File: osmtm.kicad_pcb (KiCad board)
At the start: 2 copper layers, 144.8 x 76.2 mm, 15 parts

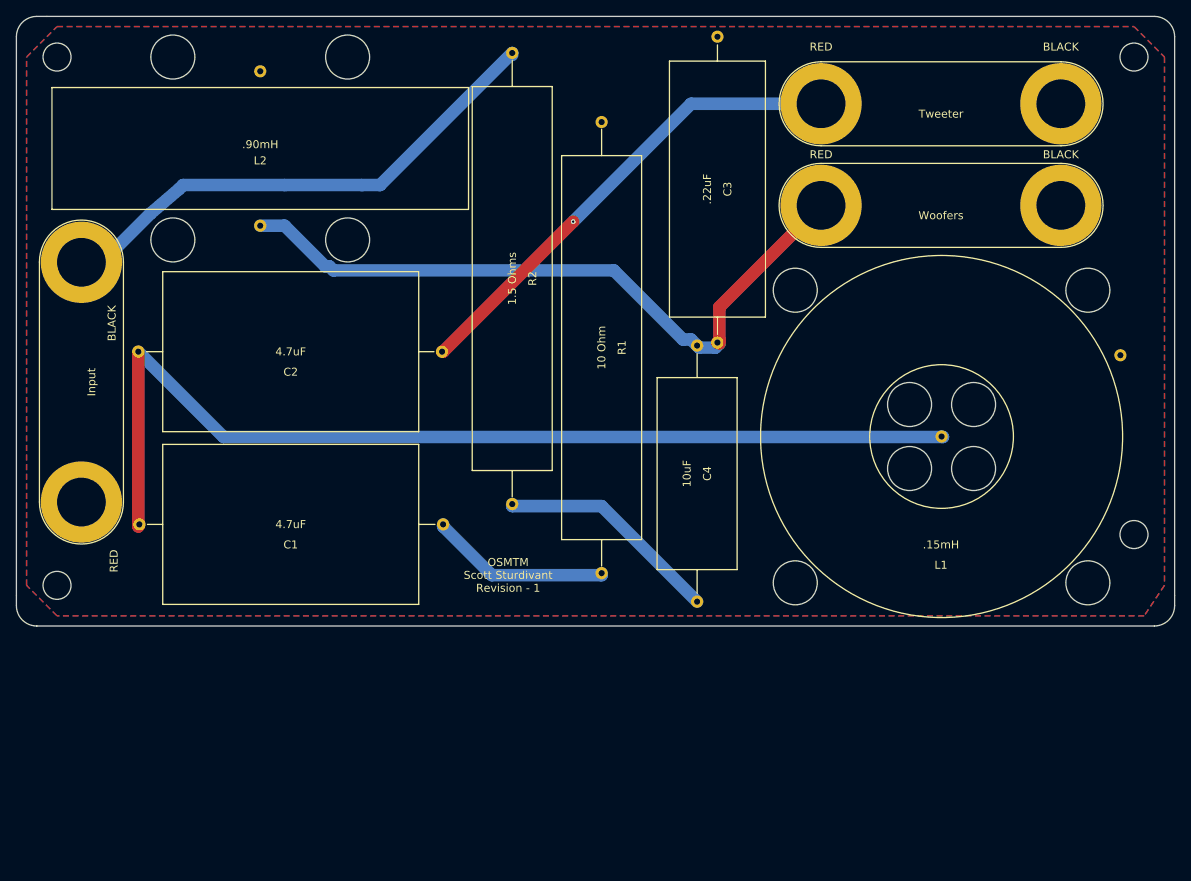
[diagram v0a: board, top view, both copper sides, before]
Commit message: Use screw terminals, increase trace width.
The trace width was incorrectly using the results for external lines
when it should have been using internal.  As a result of this (and the
screw terminal change), the inductor footprints were also modified and
the amount of zip ties used reduced.
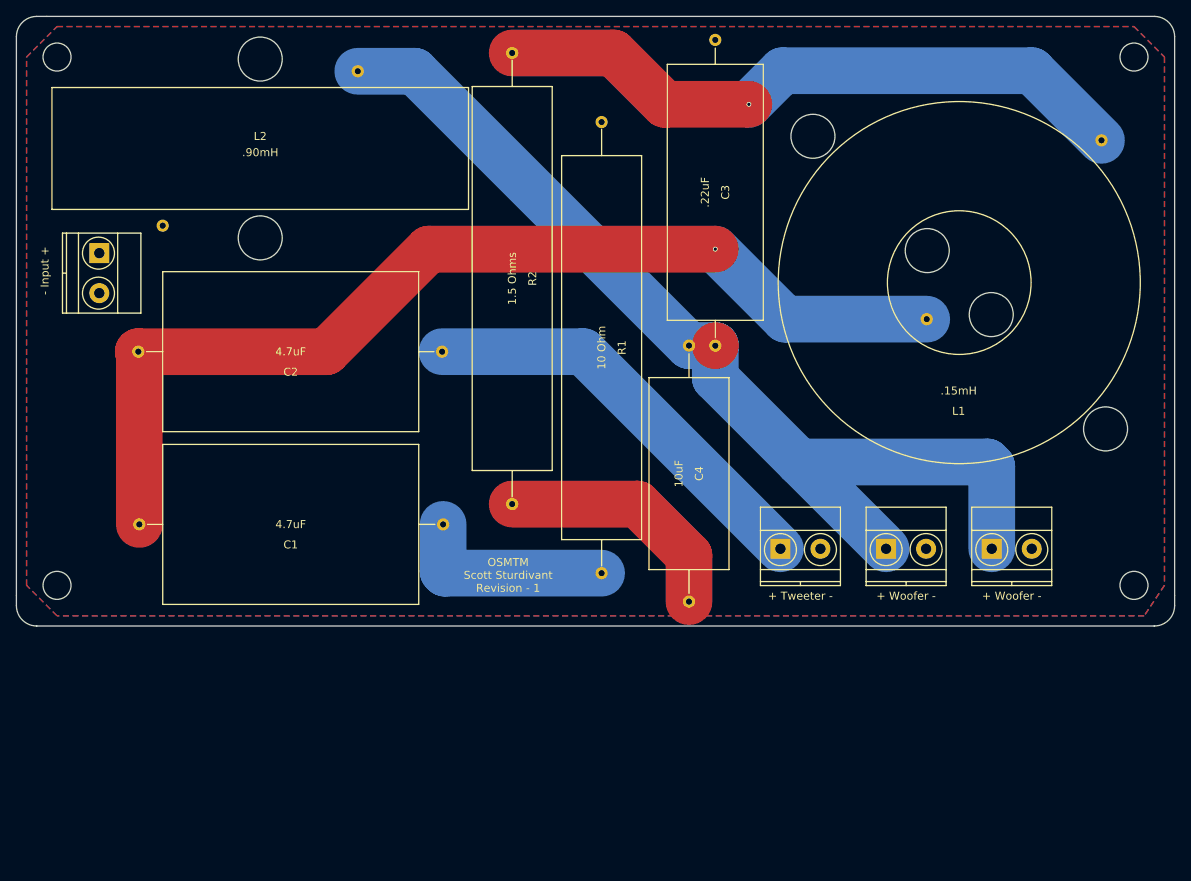
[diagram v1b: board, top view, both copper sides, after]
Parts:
- removed Input: Screw_Terminal_1x02, Connectors:Banana_Jack_2Pin
- removed Tweeter, Woofers: Speaker, Connectors:Banana_Jack_2Pin
- added + Tweeter -: Speaker, Connectors_Terminal_Blocks:TerminalBlock_Pheonix_MKDS1.5-2pol, F.Cu at (136.1, 121.2)
- added + Woofer -: Speaker, Connectors_Terminal_Blocks:TerminalBlock_Pheonix_MKDS1.5-2pol, F.Cu at (149.4, 121.2)
- added + Woofer -: Speaker, Connectors_Terminal_Blocks:TerminalBlock_Pheonix_MKDS1.5-2pol, F.Cu at (162.6, 121.2)
- added - Input +: Screw_Terminal_1x02, Connectors_Terminal_Blocks:TerminalBlock_Pheonix_MKDS1.5-2pol, F.Cu at (51.0, 84.2)
- moved L1 19.4 mm to (158.5, 87.9)
- moved REF** 6.35 mm to (180.3, 125.7)
- moved C4 1.02 mm to (124.7, 111.8)
- moved C3 0.48 mm to (128.0, 76.6)
- turned L2 to 180 degrees
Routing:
- net Net-(C3-Pad1): track 88.5 -> 127.8 mm
- net BLACK: track 64.8 -> 82.0 mm, vias 0 -> 1
- net Net-(C2-Pad1): track 60.2 -> 52.5 mm, vias 1 -> 0
- net Net-(C1-Pad2): track 22.8 -> 25.8 mm
- net Net-(C4-Pad2): track 28.3 -> 30.5 mm
- net Net-(C1-Pad1): track 127.3 -> 129.1 mm, vias 0 -> 1
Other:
- net class Default: trace_width 1.57 -> 5.84
- net class Foo: trace_width 1.57 -> 5.84
- rule trace_min: 1.5 -> 4
- board text removed: "BLACK"
- board text removed: "RED"

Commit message: Adapt board to 100mm x 100mm sizing.
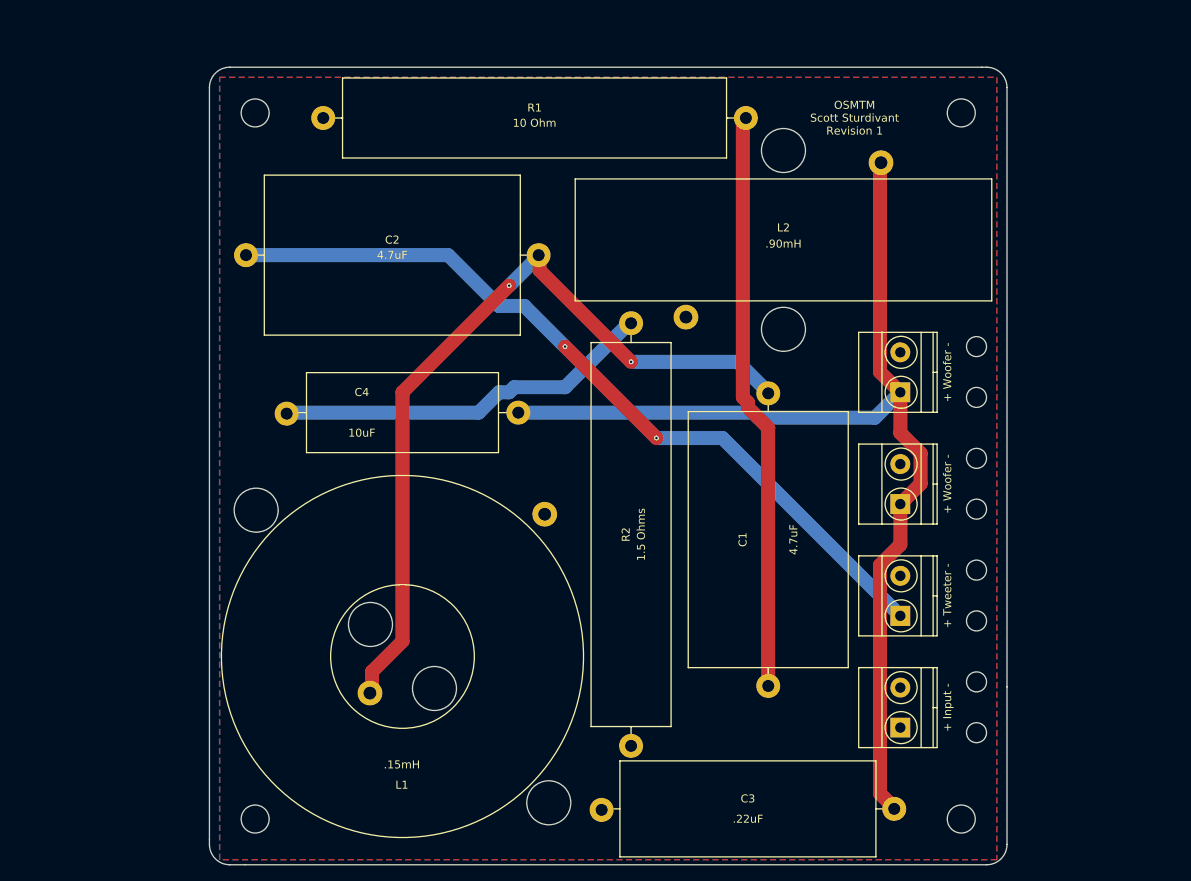
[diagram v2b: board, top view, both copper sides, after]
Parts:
- removed the + Woofer - at (149.4, 121.2)
- removed the + Woofer - at (162.6, 121.2)
- removed - Input +: Screw_Terminal_1x02, Connectors_Terminal_Blocks:TerminalBlock_Pheonix_MKDS1.5-2pol
- removed REF** (x4): MountingHole_3.5mm, Mounting_Holes:MountingHole_3.5mm
- added + Input -: Screw_Terminal_1x02, Connectors_Terminal_Blocks:TerminalBlock_Pheonix_MKDS1.5-2pol, F.Cu at (151.1, 143.5)
- added + Woofer -: Speaker, Connectors_Terminal_Blocks:TerminalBlock_Pheonix_MKDS1.5-2pol, F.Cu at (151.1, 101.6)
- added + Woofer -: Speaker, Connectors_Terminal_Blocks:TerminalBlock_Pheonix_MKDS1.5-2pol, F.Cu at (151.1, 115.6)
- added ?: , Mounting_Holes:MountingHole_3.5mm, F.Cu at (70.5, 66.7)
- added ?: , Mounting_Holes:MountingHole_2.5mm, F.Cu at (160.7, 109.9)
- added ?: , Mounting_Holes:MountingHole_2.5mm, F.Cu at (160.7, 102.2)
- added ?: , Mounting_Holes:MountingHole_2.5mm, F.Cu at (160.7, 95.9)
- added ?: , Mounting_Holes:MountingHole_3.5mm, F.Cu at (158.8, 66.7)
- added ?: , Mounting_Holes:MountingHole_3.5mm, F.Cu at (70.5, 154.9)
- added ?: , Mounting_Holes:MountingHole_3.5mm, F.Cu at (158.8, 154.9)
- added ?: , Mounting_Holes:MountingHole_2.5mm, F.Cu at (160.7, 144.1)
- added ?: , Mounting_Holes:MountingHole_2.5mm, F.Cu at (160.7, 137.8)
- added ?: , Mounting_Holes:MountingHole_2.5mm, F.Cu at (160.7, 130.2)
- added ?: , Mounting_Holes:MountingHole_2.5mm, F.Cu at (160.7, 123.8)
- added ?: , Mounting_Holes:MountingHole_2.5mm, F.Cu at (160.7, 116.2)
- C1: footprint libraries:Dayton4.7uF -> Dayton4.7uF
- C3: footprint libraries:Dayton0.22uF -> Dayton0.22uF
- C4: footprint libraries:Dayton10uFNPE -> Dayton10uFNPE
- moved L1 83.8 mm to (88.9, 134.6)
- moved C3 77.2 mm to (132.1, 153.7), turned to 180 degrees
- moved L2 66.4 mm to (136.5, 82.5)
- moved C1 59.7 mm to (134.6, 120.0), turned to 270 degrees
- moved C4 36.6 mm to (88.9, 104.1), turned to 180 degrees
- moved R2 35.3 mm to (117.5, 119.4), turned to 270 degrees
- moved R1 29.9 mm to (105.4, 67.3), turned to 180 degrees
- moved C2 17.5 mm to (87.6, 84.5), turned to 0 degrees
- moved + Tweeter - 17.2 mm to (151.1, 129.5), turned to 90 degrees
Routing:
- net BLACK: track 82.0 -> 0.00 mm, vias 1 -> 0
- net Net-(C2-Pad1): track 52.5 -> 100.5 mm, vias 0 -> 2
- net Net-(C1-Pad2): track 25.8 -> 72.8 mm
- net Net-(C1-Pad1): track 129.1 -> 100.7 mm, vias 1 -> 2
- net Net-(C4-Pad2): track 30.5 -> 48.3 mm
- net Net-(C3-Pad1): track 127.8 -> 135.3 mm
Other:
- board size 144.8 x 76.2 mm -> 99.7 x 99.7 mm
- net class Default: trace_width 5.84 -> 1.75
- net class Foo: trace_width 5.84 -> 1.75
- rule trace_min: 4 -> 1.75
- board text added: "OSMTM Scott Sturdivant Revision 1"
- board text removed: "OSMTM Scott Sturdivant Revision - 1"
